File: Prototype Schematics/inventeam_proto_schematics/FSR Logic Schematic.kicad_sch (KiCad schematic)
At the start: 37 parts, among them J4 Conn_02x20_Top_Bottom, J5 Conn_01x03, J6 Screw_Terminal_01x02, U10 TMUX1208PW, U11 MCP1525-TO, U12 OPA2333xxD, U7 MCP23S17_SP, U8 TMUX1208PW, U9 MCP23S17_SP

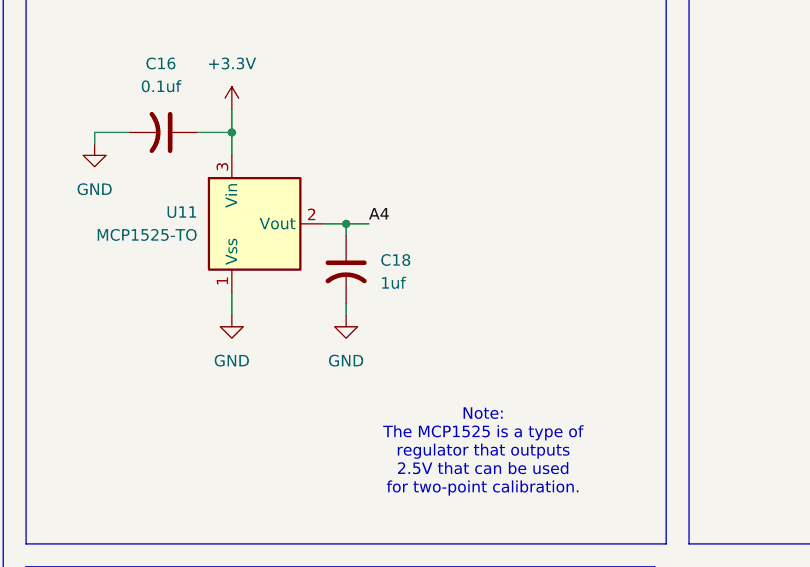
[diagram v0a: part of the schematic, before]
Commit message: Change 1uf to 10uf
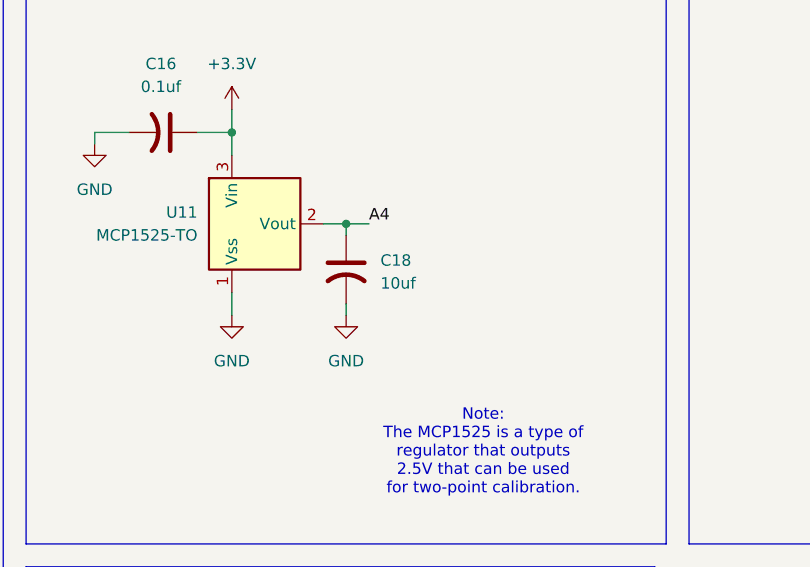
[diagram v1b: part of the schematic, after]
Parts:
- C18: value 1uf -> 10uf
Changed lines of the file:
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@@
 			)
 		)
-		(property "Value" "1uf"
+		(property "Value" "10uf"
 			(at 228.6 180.5939 0)
 			(effects

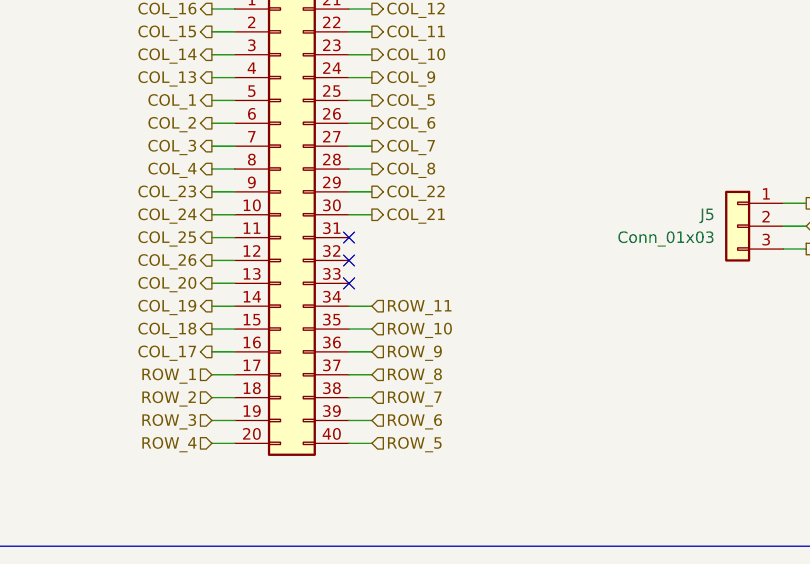
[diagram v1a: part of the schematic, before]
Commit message: Minor fix on row header
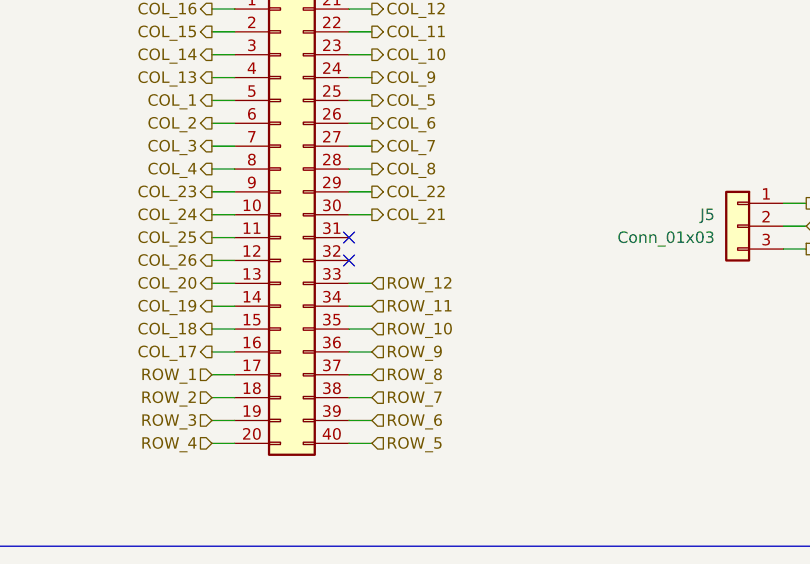
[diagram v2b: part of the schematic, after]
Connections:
- net ROW_12: now also J4.33 (Pin_33)
- no-connect marks 25 -> 24
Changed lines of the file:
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@@
 	)
 	(no_connect
-		(at 83.82 309.88)
-	)
-	(no_connect
 		(at 57.15 78.74)
 	)
@@
 	(wire
 		(pts
+			(xy 83.82 309.88) (xy 86.36 309.88)
+		)
+		(stroke
+			(width 0)
+			(type default)
+		)
+	)
+	(wire
+		(pts
 			(xy 231.14 257.81) (xy 236.22 257.81)
 		)
@@
 		)
 	)
+	(hierarchical_label "ROW_12"
+		(shape input)
+		(at 86.36 309.88 0)
+		(effects
+			(font
+				(size 1.27 1.27)
+			)
+			(justify left)
+		)
+	)

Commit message: Schematic V16
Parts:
- added C13, C16: 1nf, symbol Device:C_US
- added R329, R340: 220, symbol Device:R_US
- added R332, R346: 1M, symbol Device:R_US
- renumbered C13 to C14, C14 to C15, C15 to C17, C16 to C18, C17 to C19, C18 to C20, C20 to C21, C19 to C22, C21 to C25, C22 to C26, R329 to R330, R330 to R331, R331 to R333, R332 to R334, R333 to R335, R334 to R336, R335 to R337, R336 to R338, R337 to R339, R338 to R345, R340 to R347, R339 to R348
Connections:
- net AMP_NON_IN_1: now also C13.1, R329.2; no longer U8.8 (D)
- net AMP_NON_IN_2: now also C16.1, R340.2; no longer U10.8 (D)
- net GND: now also C13.2, C16.2, R332.2, R346.2
- new net: R329.1, R332.1, U8.8 (D)
- new net: R340.1, R346.1, U10.8 (D)
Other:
- moved on the sheet: A2, BT2, C12, C15, C18, C19, C20, C21, C22, C25, C26, F2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

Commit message: v16 minor 1
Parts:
- renumbered A2 to A5001, BT2 to BT5001, C12 to C5001, C13 to C5002, C14 to C5003, C15 to C5004, C16 to C5005, C17 to C5006, C18 to C5007, C19 to C5008, C20 to C5009, C21 to C5010, C22 to C5011, C25 to C5012, C26 to C5013, F2 to F5001, J4 to J5001, J5 to J5002, J6 to J5003, R327 to R5001, R328 to R5002, R329 to R5003, R330 to R5004, R331 to R5005, R332 to R5006, R333 to R5007, R334 to R5008, R335 to R5009, R336 to R5010, R337 to R5011, R338 to R5012, R339 to R5013, R340 to R5014, R345 to R5015, R346 to R5016, R347 to R5017, R348 to R5018, U7 to U5001, U8 to U5002, U9 to U5003, U10 to U5004, U11 to U5005, U12 to U5006
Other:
- title: (none) -> FSR Logic Schematic
